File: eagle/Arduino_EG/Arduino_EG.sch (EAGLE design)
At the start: 24 parts, among them CN1 PWR, IC1 LM358, Q1 2N7000, T1 2SA1015

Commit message: Update eagle files
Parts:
- added JP9: TP-GND, pinhead:PINHD-1X2
- C2, C4: value 22uF -> 47uF
- CN1: value PWR -> +9VPWR
- JP8: value SyncIn -> GateIn
- U$1: value ABK-PRO-MINI -> PRO-MINI; device Arduino-clone:ABK-PRO-MINI -> Arduino-clone:PRO-MINI
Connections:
- net D4: now also U$1.D5; no longer U$1.D4
- net D5: now also U$1.D6; no longer U$1.D5
- net D6: now also U$1.D7; no longer U$1.D6
- net GND: now also JP9.1, JP9.2
- net N$13: now also U$1.D3; no longer U$1.D2
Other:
- note added: "Arduino Pro Mini 16MHz/5V"
- moved on the sheet: JP8, R4

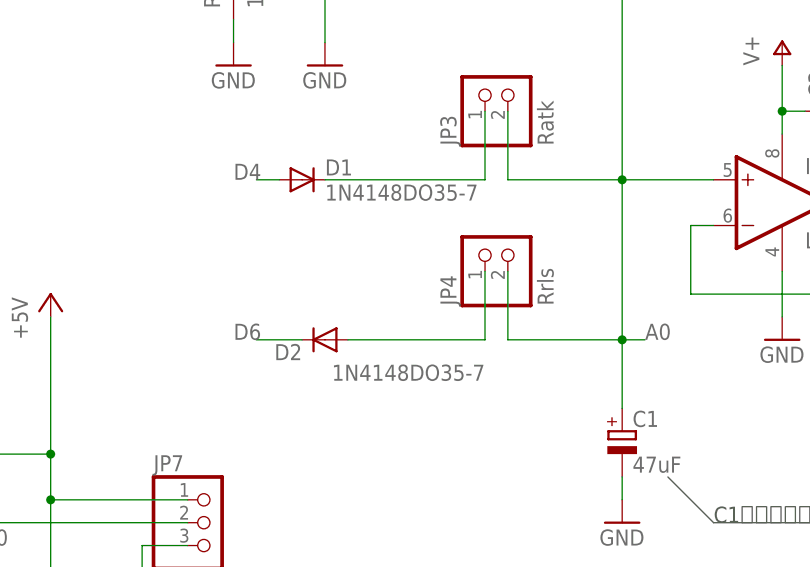
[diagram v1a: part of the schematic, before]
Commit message: Update Arduino sketch, Eagle files
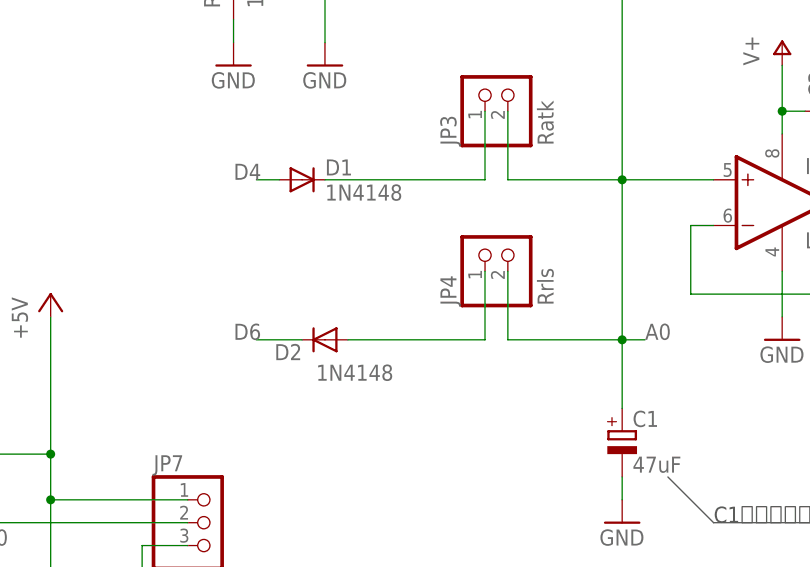
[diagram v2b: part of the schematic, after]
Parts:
- D1, D2: value 1N4148DO35-7 -> 1N4148
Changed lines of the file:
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@@
 <part name="GND1" library="supply1" library_urn="urn:adsk.eagle:library:371" deviceset="GND" device=""/>
 <part name="GND2" library="supply1" library_urn="urn:adsk.eagle:library:371" deviceset="GND" device=""/>
-<part name="D1" library="diode" library_urn="urn:adsk.eagle:library:210" deviceset="1N4148" device="DO35-7" package3d_urn="urn:adsk.eagle:package:43339/1"/>
-<part name="D2" library="diode" library_urn="urn:adsk.eagle:library:210" deviceset="1N4148" device="DO35-7" package3d_urn="urn:adsk.eagle:package:43339/1"/>
+<part name="D1" library="diode" library_urn="urn:adsk.eagle:library:210" deviceset="1N4148" device="DO35-7" package3d_urn="urn:adsk.eagle:package:43339/1" value="1N4148"/>
+<part name="D2" library="diode" library_urn="urn:adsk.eagle:library:210" deviceset="1N4148" device="DO35-7" package3d_urn="urn:adsk.eagle:package:43339/1" value="1N4148"/>
 <part name="GND3" library="supply1" library_urn="urn:adsk.eagle:library:371" deviceset="GND" device=""/>
 <part name="C1" library="rcl" library_urn="urn:adsk.eagle:library:334" deviceset="CPOL-EU" device="E2.5-7" package3d_urn="urn:adsk.eagle:package:23345/1" value="47uF"/>
@@
 <instance part="D2" gate="G$1" x="127" y="66.04" smashed="yes" rot="R180">
 <attribute name="NAME" x="124.46" y="65.5574" size="1.778" layer="95" rot="R180"/>
-<attribute name="VALUE" x="144.78" y="63.2714" size="1.778" layer="96" rot="R180"/>
+<attribute name="VALUE" x="134.62" y="63.2714" size="1.778" layer="96" rot="R180"/>
 </instance>
 <instance part="GND3" gate="1" x="160.02" y="45.72"/>

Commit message: Update eagle files
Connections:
- removed net D4: D1.A, U$1.D5
- new net D7: D2.C, U$1.D7
- net D5: now also D1.A, U$1.D5; no longer Q1.G, R2.2, U$1.D6
- net D6: now also Q1.G, R2.2, U$1.D6; no longer D2.C, U$1.D7
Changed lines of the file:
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@@
 </segment>
 </net>
-<net name="D4" class="0">
+<net name="D5" class="0">
 <segment>
 <wire x1="43.18" y1="43.18" x2="40.64" y2="43.18" width="0.1524" layer="91"/>
@@
 </segment>
 </net>
-<net name="D5" class="0">
+<net name="D6" class="0">
 <segment>
 <wire x1="43.18" y1="40.64" x2="40.64" y2="40.64" width="0.1524" layer="91"/>
@@
 </segment>
 </net>
-<net name="D6" class="0">
+<net name="D7" class="0">
 <segment>
 <wire x1="43.18" y1="38.1" x2="40.64" y2="38.1" width="0.1524" layer="91"/>
